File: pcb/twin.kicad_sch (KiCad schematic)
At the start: 68 parts, among them J1 USB_C_Receptacle_USB2.0_16P, SW1 RotaryEncoder_Switch, SW10 SW_Push_45deg, SW11 SW_Push_45deg, SW12 SW_Push_45deg, SW2 SW_Push_45deg, SW3 SW_Push_45deg, SW4 SW_Push_45deg, SW5 SW_Push_45deg, SW6 SW_Push_45deg, SW7 SW_Push_45deg, SW8 SW_Push_45deg, SW9 SW_Push_45deg, U1 ESP32-C6-MINI-1, U2 RP2040

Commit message: update pcb
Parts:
- added C13, C14: 10uf, Capacitor_SMD:C_0603_1608Metric, symbol Device:C_Small
- added C15, C16: 33pf, Capacitor_SMD:C_0603_1608Metric, symbol Device:C
- added C17: 0.1uf, Capacitor_SMD:C_0603_1608Metric, symbol Device:C_Small
- added R3, R4: 27, Resistor_SMD:R_0603_1608Metric, symbol Device:R
- added R5, R6: 1k, Resistor_SMD:R_0603_1608Metric, symbol Device:R_Small
- added R7: 10k, Resistor_SMD:R_0603_1608Metric, symbol Device:R_Small
- added SW13: SW_Push, symbol Switch:SW_Push
- added U3: MCP1700x-300xxTT, Package_TO_SOT_SMD:SOT-23, symbol Regulator_Linear:MCP1700x-300xxTT
- added U4: W25Q16JVSS, Package_SO:SOIC-8_5.3x5.3mm_P1.27mm, symbol Memory_Flash:W25Q16JVSS
- added Y1: 12MHz, symbol Device:Crystal_GND24
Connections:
- net +3V3: now also C13.1, C17.1, R7.2, U3.2 (VO), U4.8 (VCC)
- net +5V: no longer J1.A4 (VBUS), J1.A9 (VBUS), J1.B4 (VBUS), J1.B9 (VBUS)
- net D+: now also R3.1; no longer U2.47 (USB_DP)
- net D-: now also R4.1; no longer U2.46 (USB_DM)
- net GND: now also SW1.C, U2.19 (TESTEN), C13.2, C14.2, C15.1, C16.1, C17.2, SW13.1, U3.1 (GND), U4.4 (GND), Y1.2, Y1.4
- net QSPI_SCLK: now also U4.6 (CLK)
- net QSPI_SD0: now also U4.5 (DI/IO_{0})
- net QSPI_SD1: now also U4.2 (DO/IO_{1})
- net QSPI_SD2: now also U4.3 (~{WP}/IO_{2})
- net QSPI_SD3: now also U4.7 (~{HOLD}/~{RESET}/IO_{3})
- net QSPI_SS: now also R6.2, R7.1, U4.1 (~{CS})
- net XIN: now also C15.2, Y1.3
- net XOUT: now also R5.2
- net 1A: now reaches SW1.A
- net 1B: now reaches SW1.B
- new net: C16.2, R5.1, Y1.1
- new net: R3.2, U2.47 (USB_DP)
- new net: R6.1, SW13.2
- new net: R4.2, U2.46 (USB_DM)
- new net VBUS: C14.1, J1.A4 (VBUS), J1.A9 (VBUS), J1.B4 (VBUS), J1.B9 (VBUS), U3.3 (VI)
- no-connect marks 4 -> 28
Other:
- moved on the sheet: C1, C2, C3, D15, D16, D17, D18, D19, D20, D25, D26, D27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

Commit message: idek anymore i think more pcb stuff
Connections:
- net ESP-RX: now also U2.3 (GPIO1)
- net ESP-TX: now also U2.2 (GPIO0)
- no-connect marks 28 -> 26
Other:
- moved on the sheet: C15, C16, C17, D1, D10, D11, D12, D13, D14, D15, D16, D17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

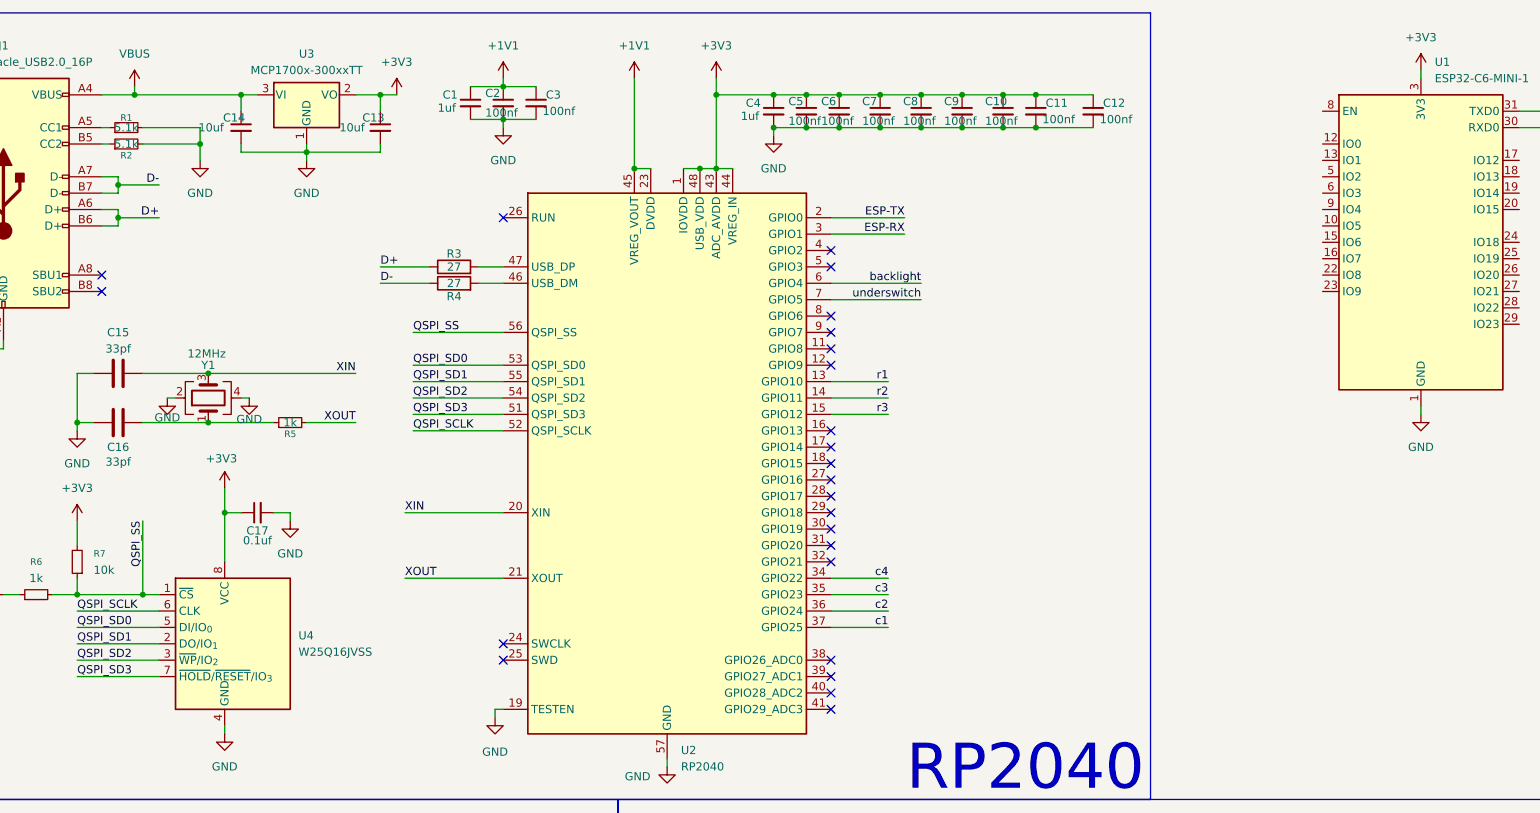
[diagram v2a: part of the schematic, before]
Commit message: Update PCB footprints and backups
Clean up PCB repository and update the board file. Removed macOS .DS_Store and a stale KiCad schematic lock, rotated twin-backups (deleted older backup zips and added new ones). Large edits to pcb/twin.kicad_pcb: reorganized net names, replaced/updated multiple footprints (added Choc keyswitch and Alps rotary encoder footprints, changed capacitor footprints/sizes, converted several pads from SMD to thru-hole), and updated 3D model paths and footprint metadata to match recent hardware/layout changes.
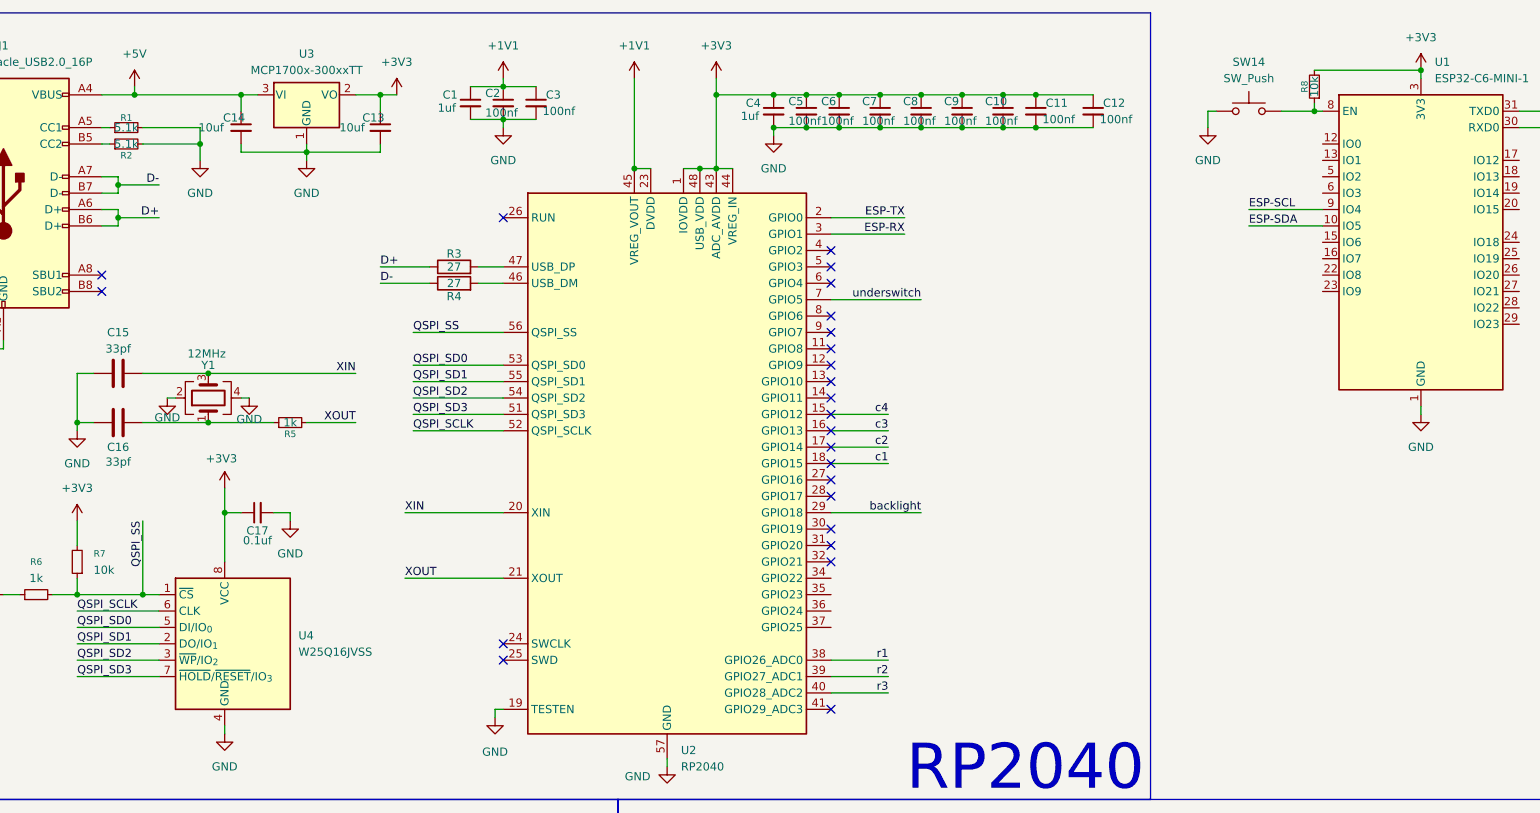
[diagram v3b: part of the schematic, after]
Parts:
- added R8: 10k, Capacitor_SMD:C_0402_1005Metric, symbol Device:R_Small
- added SW14: SW_Push, symbol Switch:SW_Push
- C1, C10, C11, C12, C13, C14, C15, C16, C17, C2, C3, C4, C5, C6, C7, C8, C9: footprint Capacitor_SMD:C_0603_1608Metric -> Capacitor_SMD:C_0402_1005Metric
- D15, D16, D17, D18, D19, D20, D25, D26, D27, D28, D29, D30, D31: footprint LED_SMD:LED_WS2812B-2020_PLCC4_2.0x2.0mm -> LED_SMD:LED_SK6812MINI-E_3.2x2.8mm_P1.5mm_ReverseMount
- R1, R2, R3, R4, R5, R6, R7: footprint Resistor_SMD:R_0603_1608Metric -> Capacitor_SMD:C_0402_1005Metric
- U4: footprint Package_SO:SOIC-8_5.3x5.3mm_P1.27mm -> Package_SON:Winbond_USON-8-1EP_3x2mm_P0.5mm_EP0.2x1.6mm
- Y1: footprint (none) -> Crystal:Crystal_SMD_3225-4Pin_3.2x2.5mm
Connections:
- net VBUS is gone; now on net +5V: C14.1, J1.A4 (VBUS), J1.A9 (VBUS), J1.B4 (VBUS), J1.B9 (VBUS), U3.3 (VI)
- net +3V3: now also R8.2
- net GND: now also SW14.1
- net backlight: now also U2.29 (GPIO18); no longer U2.6 (GPIO4)
- net c1: now also U2.18 (GPIO15); no longer U2.37 (GPIO25)
- net c2: now also U2.17 (GPIO14); no longer U2.36 (GPIO24)
- net c3: now also U2.16 (GPIO13); no longer U2.35 (GPIO23)
- net c4: now also U2.15 (GPIO12); no longer U2.34 (GPIO22)
- net r1: now also U2.38 (GPIO26_ADC0); no longer U2.13 (GPIO10)
- net r2: now also U2.39 (GPIO27_ADC1); no longer U2.14 (GPIO11)
- net r3: now also U2.40 (GPIO28_ADC2); no longer U2.15 (GPIO12)
- net ESP-SDA: now reaches U1.10 (IO5)
- net at U1.8 (EN): now also R8.1, SW14.2
- net ESP-SCL: now reaches U1.9 (IO4)

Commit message: s
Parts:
- removed D15, D16, D17, D18, D19, D20, D25, D26, D27, D28, D29, D30, D31: WS2812B-2020, LED_SMD:LED_SK6812MINI-E_3.2x2.8mm_P1.5mm_ReverseMount, symbol LED:WS2812B-2020
- added D23, D24, D25, D26, D27, D28, D34, D35, D36, D37, D38: LED_SK6812MINI, footprints:MX_SK6812MINI-E, symbol ScottoKeebs:LED_SK6812MINI
- D10: renamed from D23; footprint Diode_SMD:D_SOD-323 -> Diode_SMD:D_SOD-323_HandSoldering
- D11: renamed from D24; footprint Diode_SMD:D_SOD-323 -> Diode_SMD:D_SOD-323_HandSoldering
- D19: renamed from D32; footprint Diode_SMD:D_SOD-323 -> Diode_SMD:D_SOD-323_HandSoldering
- D20: renamed from D33; footprint Diode_SMD:D_SOD-323 -> Diode_SMD:D_SOD-323_HandSoldering
- D21: renamed from D34; footprint Diode_SMD:D_SOD-323 -> Diode_SMD:D_SOD-323_HandSoldering
- D22: renamed from D35; footprint Diode_SMD:D_SOD-323 -> Diode_SMD:D_SOD-323_HandSoldering
- D29: renamed from D36; footprint Diode_SMD:D_SOD-323 -> Diode_SMD:D_SOD-323_HandSoldering
- D30: renamed from D37; footprint Diode_SMD:D_SOD-323 -> Diode_SMD:D_SOD-323_HandSoldering
- D31: renamed from D38; footprint Diode_SMD:D_SOD-323 -> Diode_SMD:D_SOD-323_HandSoldering
- D32: renamed from D39; footprint Diode_SMD:D_SOD-323 -> Diode_SMD:D_SOD-323_HandSoldering
- D8: renamed from D21; footprint Diode_SMD:D_SOD-323 -> Diode_SMD:D_SOD-323_HandSoldering
- D9: renamed from D22; footprint Diode_SMD:D_SOD-323 -> Diode_SMD:D_SOD-323_HandSoldering
- SW1: renamed from SW14; footprint (none) -> Button_Switch_SMD:SW_Push_SPST_NO_Alps_SKRK
- SW2: renamed from SW13; footprint (none) -> Button_Switch_SMD:SW_Push_SPST_NO_Alps_SKRK
- renumbered C14 to C13, C13 to C14, D8 to D12, D9 to D13, D10 to D14, D11 to D15, D12 to D16, D13 to D17, D14 to D18, R8 to R1, R1 to R2, R2 to R3, R3 to R4, R4 to R5, R5 to R6, R6 to R8, SW8 to SW10, SW9 to SW11, SW10 to SW12, SW11 to SW13, SW12 to SW14, SW1 to SW3, SW2 to SW4, SW3 to SW5, SW4 to SW6, SW5 to SW7, SW6 to SW8, SW7 to SW9, U3 to U1, U1 to U2, U2 to U3
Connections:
- net +5V: now also D23.1 (VDD), D24.1 (VDD), D25.1 (VDD), D26.1 (VDD), D27.1 (VDD), D28.1 (VDD), D34.1 (VDD), D35.1 (VDD), D36.1 (VDD), D37.1 (VDD), D38.1 (VDD)
- net GND: now also D23.3 (VSS), D24.3 (VSS), D25.3 (VSS), D26.3 (VSS), D27.3 (VSS), D28.3 (VSS), D34.3 (VSS), D35.3 (VSS), D36.3 (VSS), D37.3 (VSS), D38.3 (VSS)
- net underswitch: now also D23.4 (DIN)
- new net: D36.4 (DIN), D37.2 (DOUT)
- new net: D37.4 (DIN), D38.2 (DOUT)
- new net: D35.4 (DIN), D36.2 (DOUT)
- new net: D26.2 (DOUT), D27.4 (DIN)
- new net: D25.2 (DOUT), D26.4 (DIN)
- new net: D23.2 (DOUT), D24.4 (DIN)
- new net: D27.2 (DOUT), D28.4 (DIN)
- new net: D24.2 (DOUT), D25.4 (DIN)
- new net: D28.2 (DOUT), D38.4 (DIN)
- new net: D34.4 (DIN), D35.2 (DOUT)

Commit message: loads of stuff
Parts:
- added C18, C19, C21, C22, C23: 100nf, Capacitor_SMD:C_0402_1005Metric, symbol Device:C_Small
- added C20: 1uf, Capacitor_SMD:C_0402_1005Metric, symbol Device:C_Small
- added H1, H2, H3, H4: MountingHole_Pad, MountingHole:MountingHole_2.2mm_M2_DIN965_Pad, symbol Mechanical:MountingHole_Pad
- added J2: ESP FLASH, Connector_PinHeader_2.54mm:PinHeader_1x04_P2.54mm_Vertical, symbol Connector:Conn_01x04_Pin
- added R10, R13, R9: 10k, Capacitor_SMD:C_0402_1005Metric, symbol Device:R_Small
- added R11, R12: 47, Capacitor_SMD:C_0402_1005Metric, symbol Device:R_Small
- added SW15, SW16: BOOT, Button_Switch_SMD:SW_Push_SPST_NO_Alps_SKRK, symbol Switch:SW_SPST
- C17: value 0.1uf -> 100nf
- SW10, SW11, SW12, SW13, SW14, SW4, SW5, SW6, SW7, SW8, SW9: value SW_Push_45deg -> Choc
- U1: value MCP1700x-300xxTT -> MCP1700x-330xxTT; symbol Regulator_Linear:MCP1700x-300xxTT -> Regulator_Linear:MCP1700x-330xxTT
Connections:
- net +3V3: now also C20.1, C21.1, J2.1 (Pin_1), R10.2, R13.2, R9.2
- net 1A: now also U3.7 (GPIO5), C18.1
- net 1B: now also U3.8 (GPIO6), C19.1
- net ESP-RX: now also J2.3 (Pin_3), R12.1; no longer U2.30 (RXD0)
- net ESP-TX: now also J2.2 (Pin_2), R11.2; no longer U2.31 (TXD0)
- net GND: now also C18.2, C19.2, C20.2, C21.2, C22.2, C23.2, H1.1, J2.4 (Pin_4), SW15.1 (A), SW16.1 (A)
- net r1: now also U3.12 (GPIO9); no longer U3.38 (GPIO26_ADC0)
- net r2: now also U3.13 (GPIO10); no longer U3.39 (GPIO27_ADC1)
- net r3: now also U3.14 (GPIO11); no longer U3.40 (GPIO28_ADC2)
- net underswitch: now also U3.9 (GPIO7); no longer U3.7 (GPIO5)
- net at R1.1, SW1.2, U2.8 (EN): now also C23.1
- net at U3.26 (RUN): now also R13.1, SW16.2 (B)
- net at U2.22 (IO8): now also R10.1
- net at U2.23 (IO9): now also C22.1, R9.1, SW15.2 (B)
- new net: R12.2, U2.30 (RXD0)
- new net: R11.1, U2.31 (TXD0)
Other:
- moved on the sheet: C1, C10, C11, C12, C15, C16, C17, C2, C3, C4, C5, C6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
